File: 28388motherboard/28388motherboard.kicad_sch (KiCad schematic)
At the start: 180 parts, among them CN1 DB141V-2.54-6P, CN2 DB141V-2.54-6P, J1 Conn_02x02_Top_Bottom, J10 PM2.54-2*10, J11 Conn_02x10_Top_Bottom, J12 Conn_02x10_Top_Bottom, J13 Conn_02x02_Counter_Clockwise, J14 Conn_02x02_Counter_Clockwise, J15 2.54-2*5, J16 2.54-2*5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

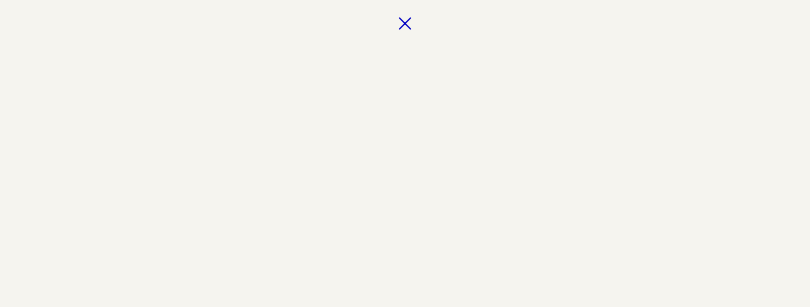
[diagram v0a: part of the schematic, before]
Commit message: 修改了half bridge的PWM 反了的bug
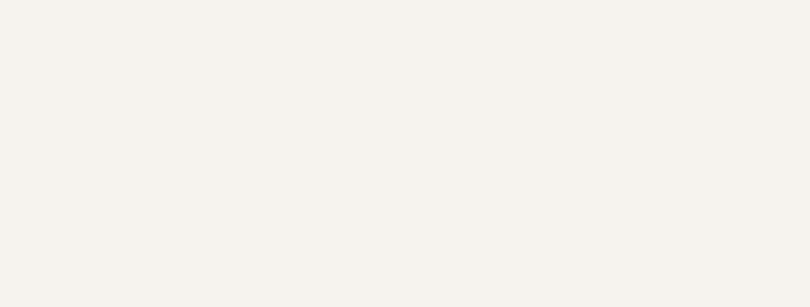
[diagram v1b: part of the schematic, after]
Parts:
- J2, J3, J4, J5: value ~ -> (none)
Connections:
- no-connect marks 45 -> 44

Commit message: 修改部分bug
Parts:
- removed J9: 2.54-2*5, Lib_sheet_10:HDR-TH_10P-P2.54-V-F-R2-C5-S2.54, symbol sheet1-altium-import:2.54-2*5_2
- removed TP_5V1: TestPoint, TestPoint:TestPoint_Pad_1.0x1.0mm, symbol Connector:TestPoint
- added J7, J8: Conn_01x01, TestPoint:TestPoint_Pad_3.0x3.0mm, symbol Connector_Generic:Conn_01x01
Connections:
- net GND: now also J8.1 (Pin_1)
- net Header-D+5V: now also J7.1 (Pin_1)
